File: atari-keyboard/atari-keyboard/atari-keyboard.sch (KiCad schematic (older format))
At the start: 129 parts, among them SW1 MENU, SW10 2, SW11 0, SW12 E, SW13 [-], SW14 G, SW15 CAPS, SW16 M, SW17 RESET, SW18 3, SW19 <, SW2 1, SW20 R, SW21 [=], SW22 H, SW23 LSHIFT, SW24 [,], SW25 OPTION, SW26 4, SW27 >, SW28 T, SW29 RET, SW3 9, SW30 J, SW31 Z, SW32 [.], SW33 SELECT, SW34 5, SW35 BS, SW36 Y, SW37 CTRL, SW38 K, SW39 X, SW4 W, SW40 [/], SW41 START, SW42 6, SW43 BRK, SW44 U, SW45 A, SW46 L, SW47 C, SW48 RSHIFT, SW49 HELP, SW5 P, SW50 7, SW51 TAB, SW52 I, SW53 S, SW54 [;], SW55 V, SW56 INV, SW57 ESC, SW58 8, SW59 Q, SW6 F, SW60 O, SW61 D, SW62 [+], SW63 B, SW64 SPC, SW7 MULT, SW8 N, SW9 TURBO, U1 ProMicro

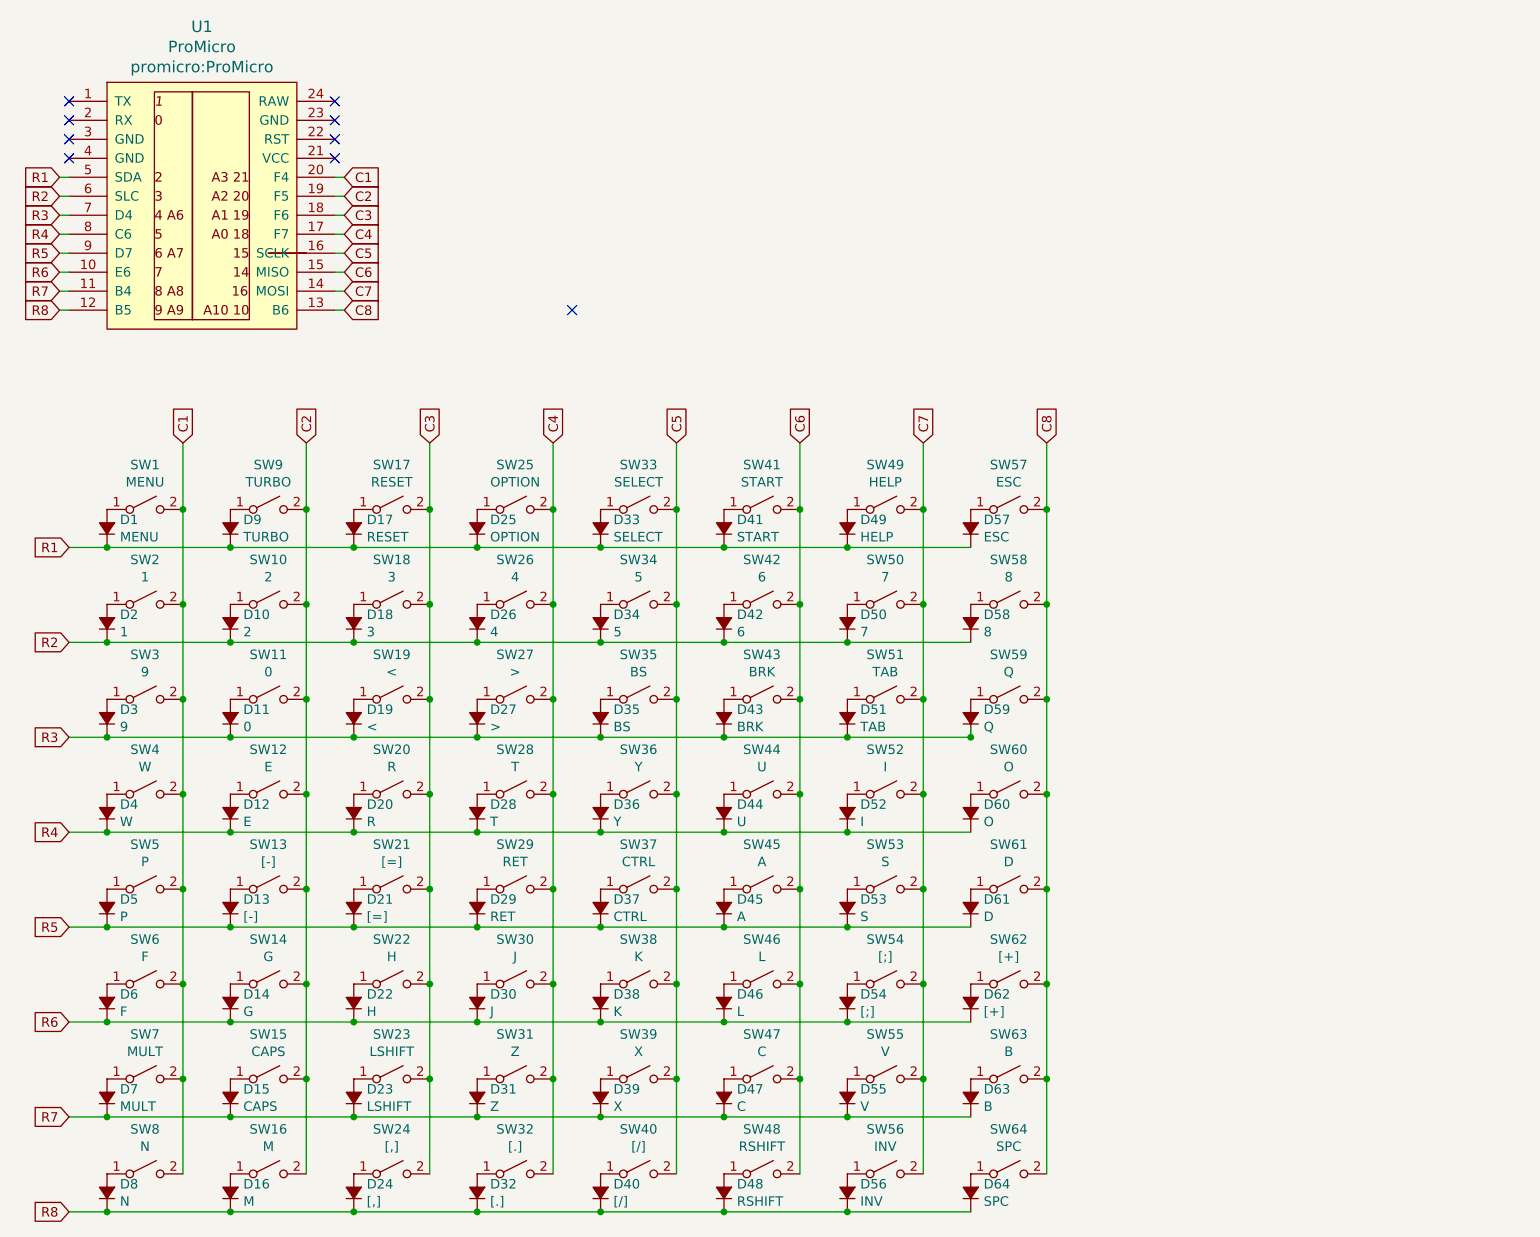
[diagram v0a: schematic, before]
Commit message: Updated atarikeyboard shift and FN key
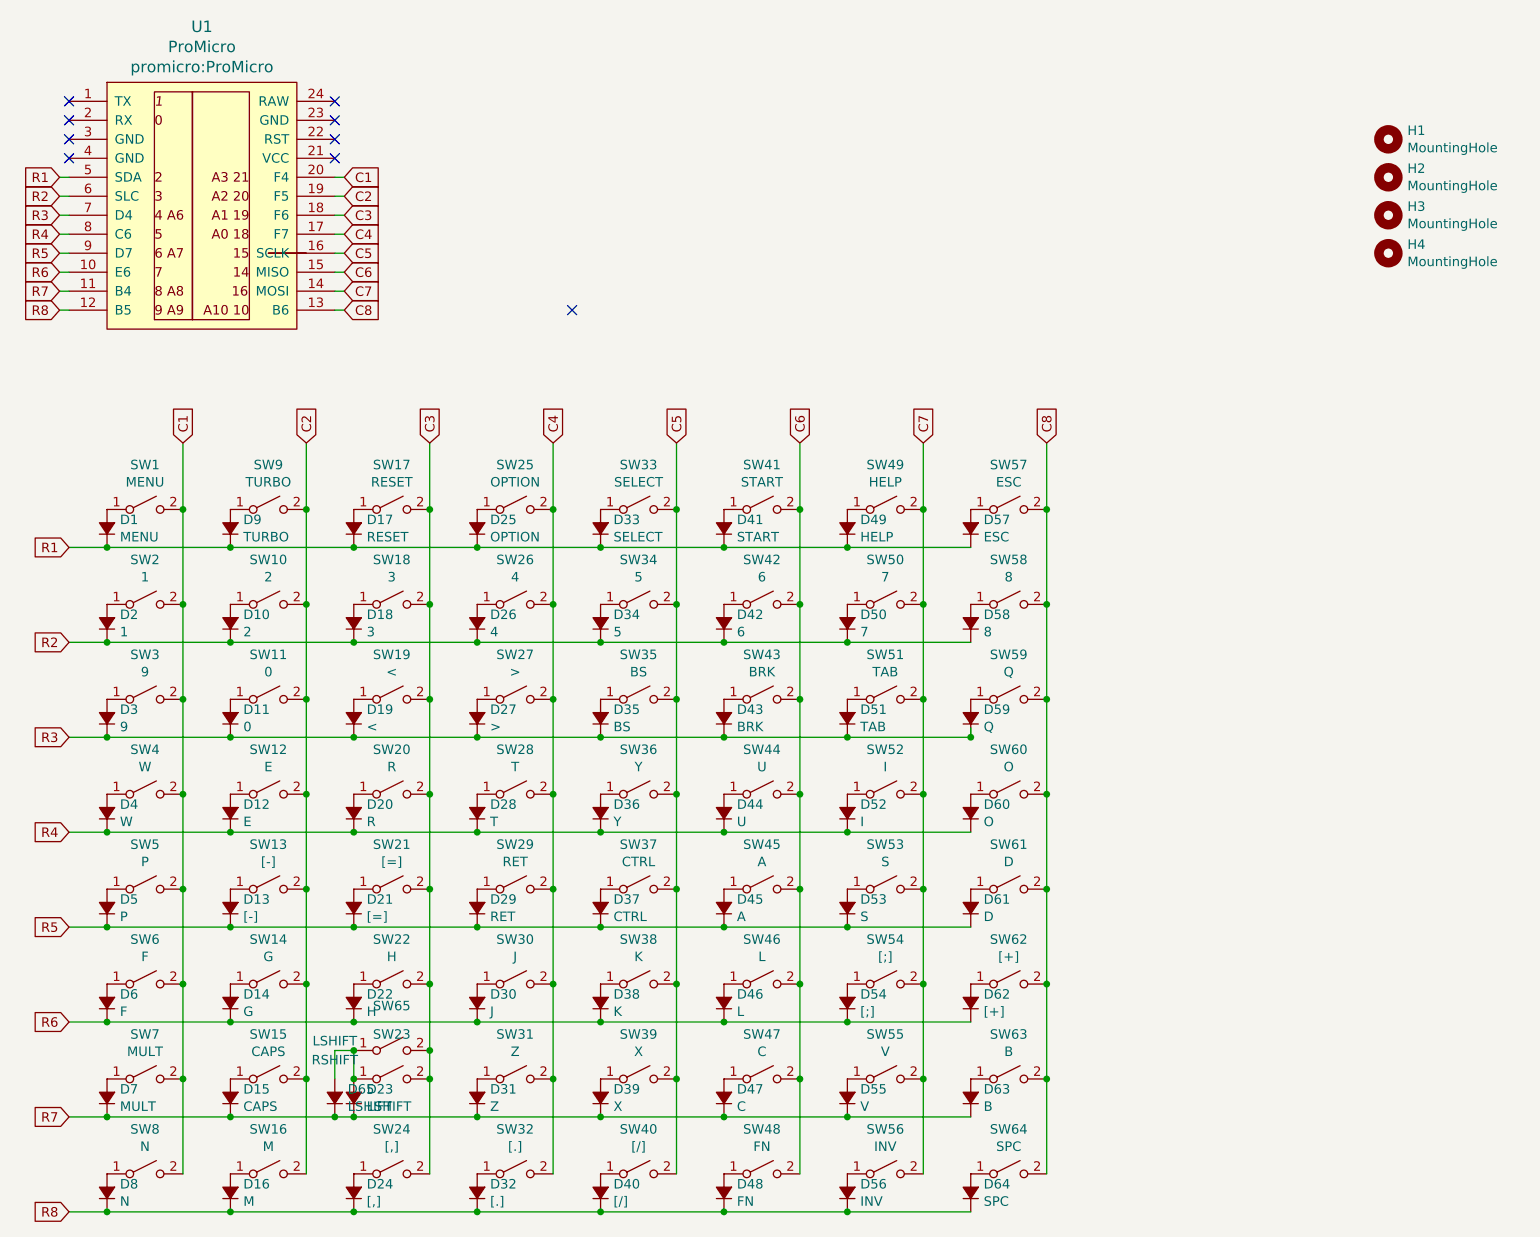
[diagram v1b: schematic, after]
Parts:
- added D65: LSHIFT, Diode_THT:D_A-405_P7.62mm_Horizontal, symbol Device:D_Small_ALT
- added H1, H2, H3, H4: MountingHole, MountingHole:MountingHole_3.2mm_M3, symbol Mechanical:MountingHole
- added SW65: RSHIFT, Button_Switch_Keyboard:SW_Cherry_MX_1.75u_PCB, symbol Switch:SW_SPST
- D48, SW48: value RSHIFT -> FN
- SW64: footprint Button_Switch_Keyboard:SW_Cherry_MX_1.00u_PCB -> Button_Switch_Keyboard:SW_Cherry_MX_6.25u_PCB
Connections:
- net C3: now also SW65.2 (B)
- net R7: now also D65.1 (K)
- net at D23.2 (A), SW23.1 (A): now also D65.2 (A), SW65.1 (A)
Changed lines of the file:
@@
-$EndComp
-$Comp
-L Device:D_Small_ALT D57
-U 1 1 5FCAE6BE
-P 5800 3550
-F 0 "D57" V 5846 3482 50  0000 R CNN
-F 1 "ESC" V 5755 3482 50  0000 R CNN
-F 2 "Diode_THT:D_A-405_P7.62mm_Horizontal" V 5800 3550 50  0001 C CNN
-F 3 "~" V 5800 3550 50  0001 C CNN
-	1    5800 3550
-	0    -1   -1   0
 $EndComp
 $Comp
@@
 P 4500 7050
 F 0 "D48" V 4546 6982 50  0000 R CNN
-F 1 "RSHIFT" V 4455 6982 50  0000 R CNN
+F 1 "FN" V 4455 6982 50  0000 R CNN
 F 2 "Diode_THT:D_A-405_P7.62mm_Horizontal" V 4500 7050 50  0001 C CNN
 F 3 "~" V 4500 7050 50  0001 C CNN
@@
 P 2750 6450
 F 0 "SW23" H 2750 6685 50  0000 C CNN
-F 1 "LSHIFT" H 2750 6594 50  0000 C CNN
+F 1 "LSHIFT" H 2450 6650 50  0000 C CNN
 F 2 "Button_Switch_Keyboard:SW_Cherry_MX_2.25u_PCB" H 2750 6450 50  0001 C CNN
 F 3 "~" H 2750 6450 50  0001 C CNN
@@
 P 4700 6950
 F 0 "SW48" H 4700 7185 50  0000 C CNN
-F 1 "RSHIFT" H 4700 7094 50  0000 C CNN
+F 1 "FN" H 4700 7094 50  0000 C CNN
 F 2 "Button_Switch_Keyboard:SW_Cherry_MX_1.75u_PCB" H 4700 6950 50  0001 C CNN
 F 3 "~" H 4700 6950 50  0001 C CNN
@@
 F 0 "SW64" H 6000 7185 50  0000 C CNN
 F 1 "SPC" H 6000 7094 50  0000 C CNN
-F 2 "Button_Switch_Keyboard:SW_Cherry_MX_1.00u_PCB" H 6000 6950 50  0001 C CNN
+F 2 "Button_Switch_Keyboard:SW_Cherry_MX_6.25u_PCB" H 6000 6950 50  0001 C CNN
 F 3 "~" H 6000 6950 50  0001 C CNN
 	1    6000 6950
@@
 Connection ~ 5150 3650
 Wire Wire Line
-	5150 3650 5800 3650
-Wire Wire Line
 	1050 4150 1250 4150
 Connection ~ 1250 4150
@@
 Connection ~ 1900 6650
 Wire Wire Line
-	1900 6650 2550 6650
+	1900 6650 2450 6650
 Connection ~ 2550 6650
 Wire Wire Line
@@
 Connection ~ 2950 5950
 Wire Wire Line
-	2950 5950 2950 6450
+	2950 5950 2950 6300
 Connection ~ 2950 6450
 Wire Wire Line
@@
 NoConn ~ 1050 1600
 NoConn ~ 3700 2400
+$Comp
+L Mechanical:MountingHole H1
+U 1 1 5FFF9FD0
+P 8000 1500
+F 0 "H1" H 8100 1546 50  0000 L CNN
+F 1 "MountingHole" H 8100 1455 50  0000 L CNN
+F 2 "MountingHole:MountingHole_3.2mm_M3" H 8000 1500 50  0001 C CNN
+F 3 "~" H 8000 1500 50  0001 C CNN
+	1    8000 1500
+	1    0    0    -1
+$EndComp
+$Comp
+L Mechanical:MountingHole H2
+U 1 1 5FFFA140
+P 8000 1700
+F 0 "H2" H 8100 1746 50  0000 L CNN
+F 1 "MountingHole" H 8100 1655 50  0000 L CNN
+F 2 "MountingHole:MountingHole_3.2mm_M3" H 8000 1700 50  0001 C CNN
+F 3 "~" H 8000 1700 50  0001 C CNN
+	1    8000 1700
+	1    0    0    -1
+$EndComp
+$Comp
+L Mechanical:MountingHole H3
+U 1 1 5FFFA55B
+P 8000 1900
+F 0 "H3" H 8100 1946 50  0000 L CNN
+F 1 "MountingHole" H 8100 1855 50  0000 L CNN
+F 2 "MountingHole:MountingHole_3.2mm_M3" H 8000 1900 50  0001 C CNN
+F 3 "~" H 8000 1900 50  0001 C CNN
+	1    8000 1900
+	1    0    0    -1
+$EndComp
+$Comp
+L Mechanical:MountingHole H4
+U 1 1 5FFFA77E
+P 8000 2100
+F 0 "H4" H 8100 2146 50  0000 L CNN
+F 1 "MountingHole" H 8100 2055 50  0000 L CNN
+F 2 "MountingHole:MountingHole_3.2mm_M3" H 8000 2100 50  0001 C CNN
+F 3 "~" H 8000 2100 50  0001 C CNN
+	1    8000 2100
+	1    0    0    -1
+$EndComp
+$Comp
+L Switch:SW_SPST SW65
+U 1 1 60197888
+P 2750 6300
+F 0 "SW65" H 2750 6535 50  0000 C CNN
+F 1 "RSHIFT" H 2450 6250 50  0000 C CNN
+F 2 "Button_Switch_Keyboard:SW_Cherry_MX_1.75u_PCB" H 2750 6300 50  0001 C CNN
+F 3 "~" H 2750 6300 50  0001 C CNN
+	1    2750 6300
+	1    0    0    -1
+$EndComp
+Connection ~ 2950 6300
+Wire Wire Line
+	2950 6300 2950 6450
+Wire Wire Line
+	2550 6300 2550 6450
+Connection ~ 2550 6450
+Wire Wire Line
+	5150 3650 5800 3650
+$Comp
+L Device:D_Small_ALT D57
+U 1 1 601ACCD9
+P 5800 3550
+F 0 "D57" V 5846 3482 50  0000 R CNN
+F 1 "ESC" V 5755 3482 50  0000 R CNN
+F 2 "Diode_THT:D_A-405_P7.62mm_Horizontal" V 5800 3550 50  0001 C CNN
+F 3 "~" V 5800 3550 50  0001 C CNN
+	1    5800 3550
+	0    -1   -1   0
+$EndComp
+$Comp
+L Device:D_Small_ALT D65
+U 1 1 601C9222
+P 2450 6550
+F 0 "D65" V 2496 6482 50  0000 R CNN
+F 1 "LSHIFT" V 2405 6482 50  0000 R CNN
+F 2 "Diode_THT:D_A-405_P7.62mm_Horizontal" V 2450 6550 50  0001 C CNN
+F 3 "~" V 2450 6550 50  0001 C CNN
+	1    2450 6550
+	0    -1   -1   0
+$EndComp
+Connection ~ 2450 6650
+Wire Wire Line
+	2450 6650 2550 6650
+Wire Wire Line
+	2550 6300 2450 6300
+Wire Wire Line
+	2450 6300 2450 6450
+Connection ~ 2550 6300
 $EndSCHEMATC
